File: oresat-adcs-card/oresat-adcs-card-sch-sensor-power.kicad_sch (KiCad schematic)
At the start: 83 parts, among them Q26 MOSFET-PCH-SOT23-6, Q27 MOSFET-PCH-SOT23-6, Q28 PMV45EN2R, Q29 PMV45EN2R, U29 MAX7310ATE, U30 MAX4211FETE, U31 TPS62111RSA, U32 MIC842LYC5-TR, U33 MIC842LYC5-TR

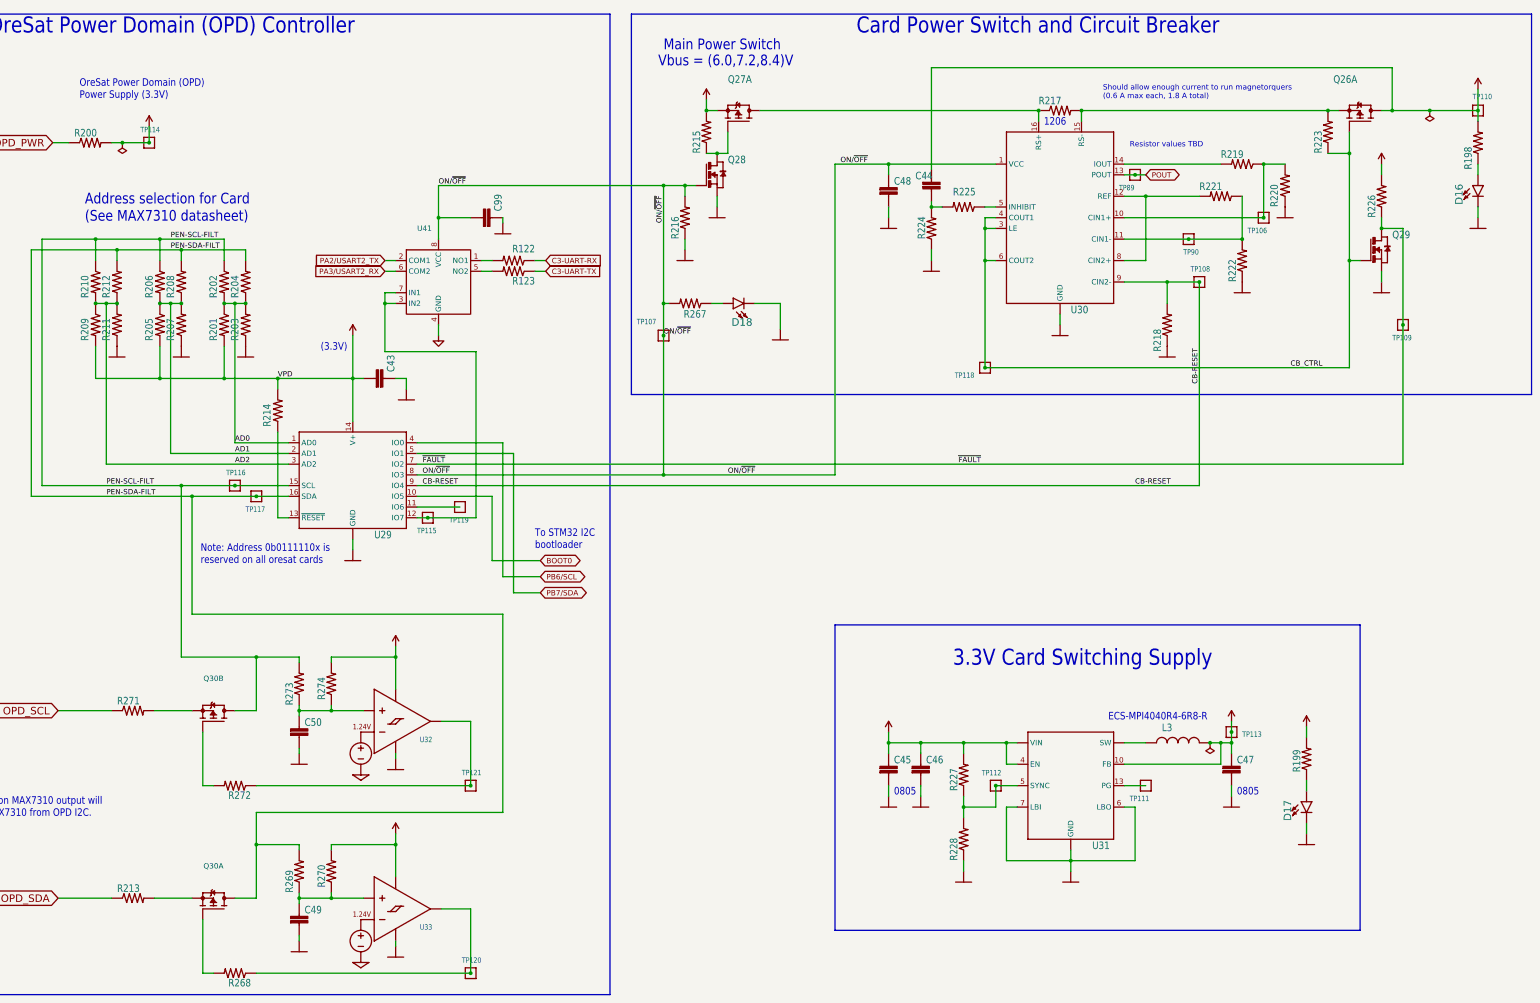
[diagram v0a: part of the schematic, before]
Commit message: Design review changes
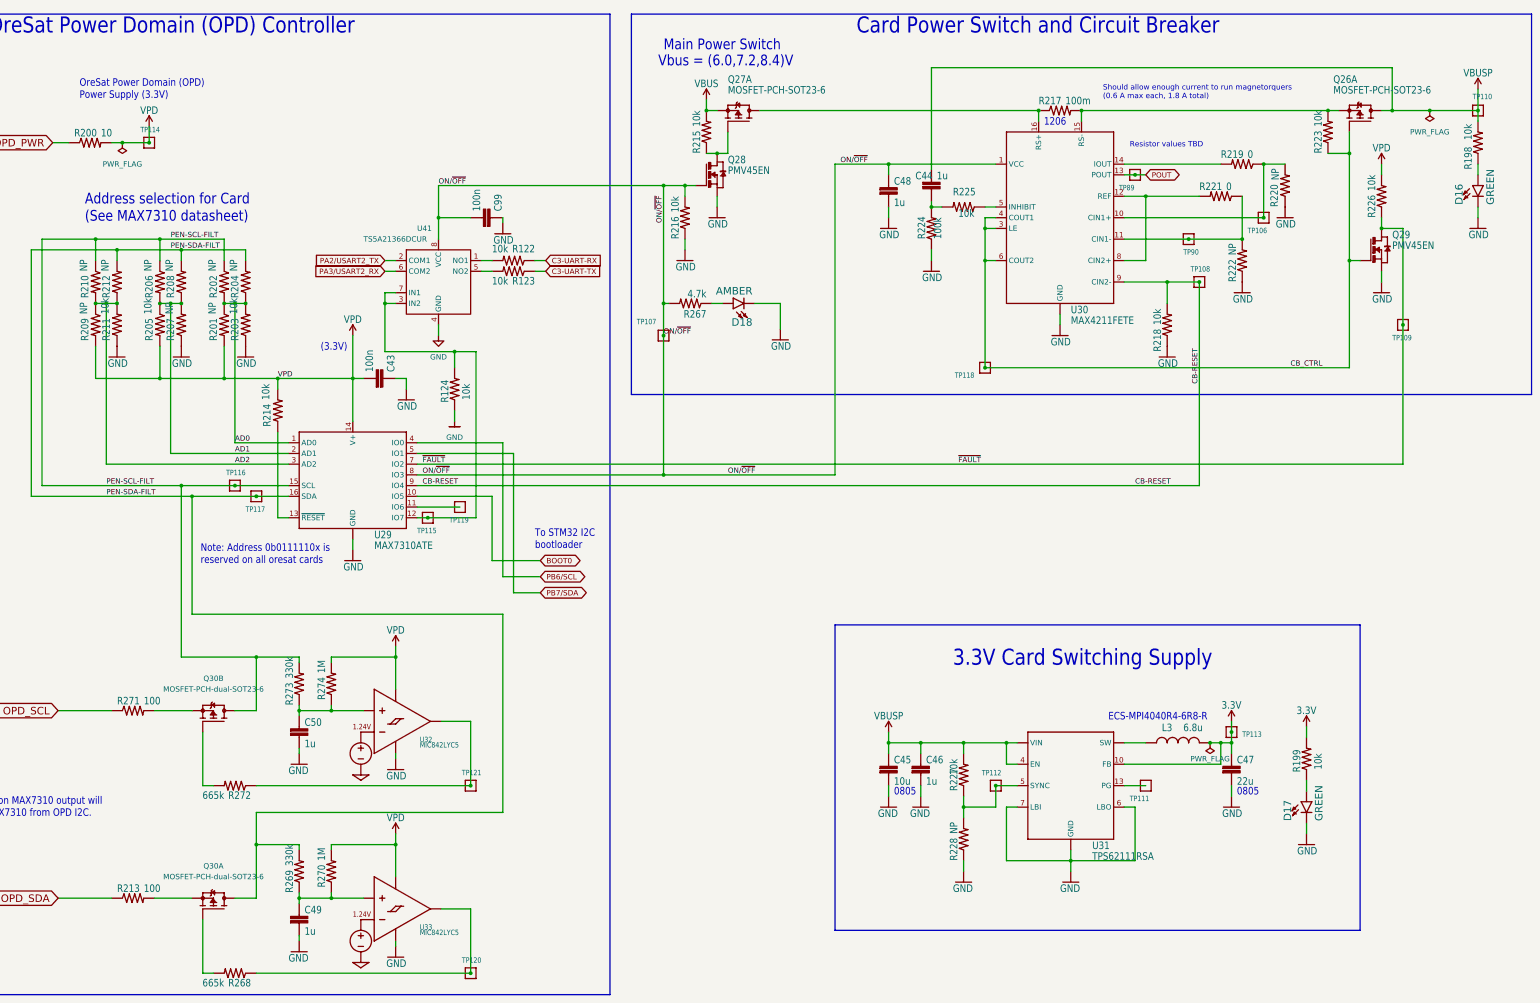
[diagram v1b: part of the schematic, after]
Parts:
- added R124: CRGCQ0603F2K7, oresat-acs-card:.0603-C-NOSILK, symbol oresat-acs-card-eagle-import:R-US_0603-C-NOSILK
- C43, C46, C48, C49, C50, C99, R122, R123, R198, R199, R200, R201, R202, R203, R204, R205, R206, R207, R208, R209, R210, R211, R212, R213, R214, R215, R216, R218, R219, R220, R221, R222, R223, R224, R225, R226, R227, R228, R267, R268, R269, R270, R271, R272, R273, R274: footprint (none) -> oresat-acs-card:.0603-C-NOSILK
- C44: value (none) -> 1u; footprint (none) -> oresat-acs-card:.0603-C-NOSILK
- C45, C47: footprint (none) -> oresat-acs-card:.0805-B-NOSILK
- D16, D17, D18: footprint (none) -> oresat-acs-card:LED-0603
- L3: footprint (none) -> oresat-acs-card:ECS-MPI4040
- Q26, Q27: footprint (none) -> oresat-acs-card:SOT23-6
- Q28, Q29: footprint (none) -> oresat-acs-card:SOT23
- Q30: value (none) -> MOSFET-PCH-dual-SOT23-6; footprint (none) -> oresat-acs-card:SOT23-6
- R217: footprint (none) -> oresat-acs-card:R1206
- TP106, TP107, TP108, TP109, TP110, TP111, TP112, TP113, TP114, TP115, TP116, TP117, TP118, TP119, TP120, TP121, TP89, TP90: value (none) -> TEST-POINT-LARGE-SQUARE; footprint (none) -> oresat-acs-card:1X01
- U29, U30: footprint (none) -> oresat-acs-card:QFN65P400X400X80-17T210
- U31: footprint (none) -> oresat-acs-card:S-PVQFN-16
- U32, U33: footprint (none) -> oresat-acs-card:SC70-5
- U41: value (none) -> TS5A21366DCUR; footprint (none) -> oresat-acs-card:DCU-R-PDSO-G8
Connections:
- net GND: now also R124.1
- net at TP115.1, U29.12 (IO7), U41.3 (IN2)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: now also R124.2

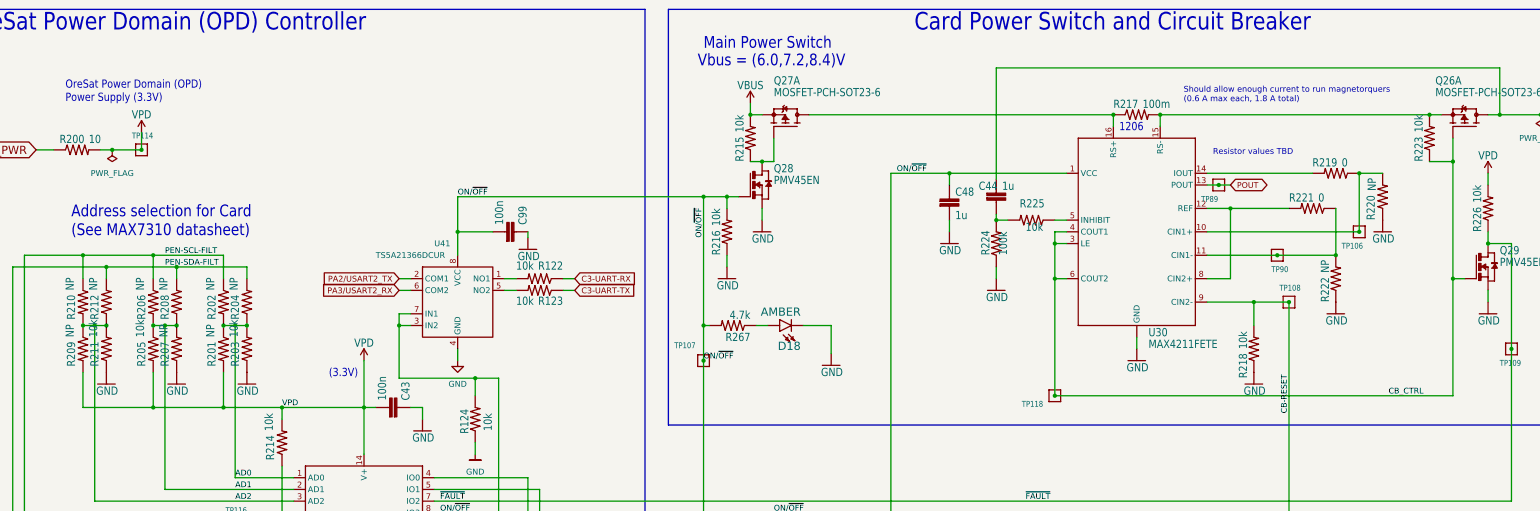
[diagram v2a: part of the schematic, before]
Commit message: Updated MT OPD breaker current limiting, and added OPD addresses to schematic
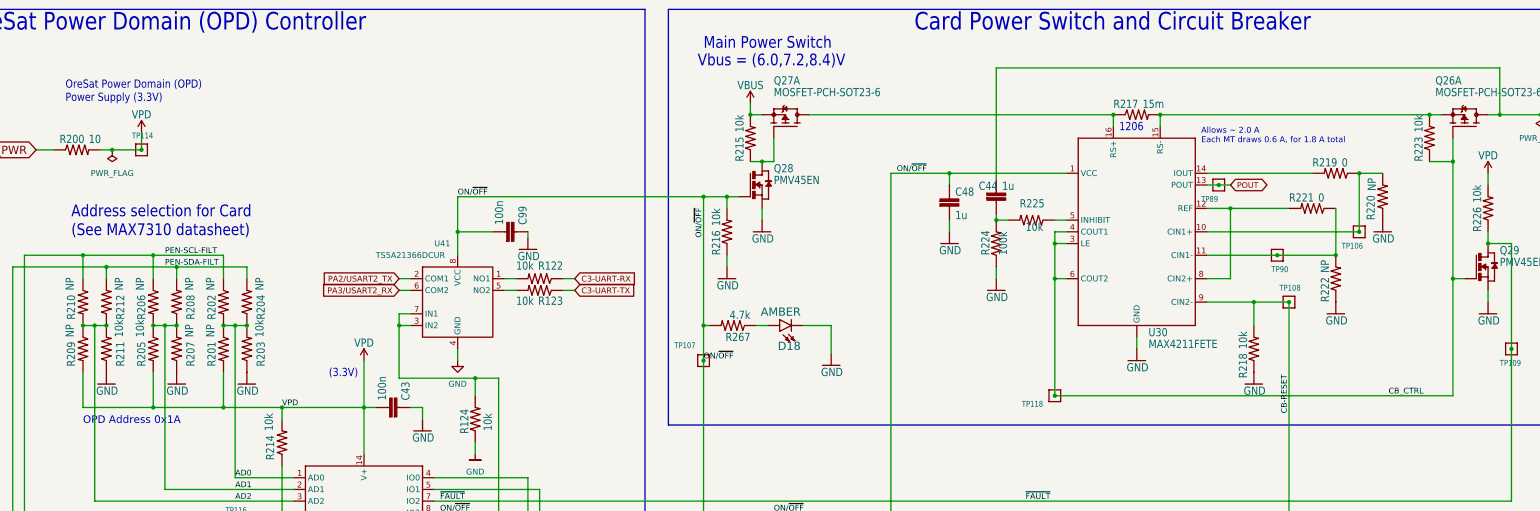
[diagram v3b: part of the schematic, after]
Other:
- note added: "Allows ~ 2.0 A Each MT draws 0.6 A, for 1.8 A total"
- note added: "OPD Address 0x1A"
- note removed: "Resistor values TBD"
- note removed: "Should allow enough current to run magnetorquers (0.6 A max each, 1.8 A total)"
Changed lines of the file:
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@@
     (stroke (width 0) (type default) (color 0 0 0 0))
+  )
+  (text "OPD Address 0x1A" (at 69.85 105.41 0)
+    (effects (font (size 1.651 1.651)) (justify left bottom))
   )
   (text "Vbus = (6.0,7.2,8.4)V" (at 203.2 27.94 180)
@@
     (effects (font (size 1.778 1.5113)) (justify left bottom))
   )
-  (text "Should allow enough current to run magnetorquers\n(0.6 A max each, 1.8 A total)"
-    (at 308.61 35.56 0)
+  (text "Allows ~ 2.0 A\nEach MT draws 0.6 A, for 1.8 A total"
+    (at 312.42 44.45 0)
     (effects (font (size 1.27 1.27)) (justify left bottom))
   )
@@
   (text "To STM32 I2C\nbootloader" (at 173.99 142.24 180)
     (effects (font (size 1.778 1.5113)) (justify left bottom))
-  )
-  (text "Resistor values TBD" (at 314.96 46.99 0)
-    (effects (font (size 1.27 1.27)) (justify left bottom))
   )
   (text "Address selection for Card\n(See MAX7310 datasheet)"
@@
   (symbol (lib_id "oresat-acs-card-eagle-import:R-US_0603-C-NOSILK") (at 90.17 78.74 90) (unit 1)
     (in_bom yes) (on_board yes)
-    (property "Reference" "R208" (id 0) (at 88.6714 82.55 0)
-      (effects (font (size 1.778 1.5113)) (justify left bottom))
-    )
-    (property "Value" "NP" (id 1) (at 88.392 76.2 0)
+    (property "Reference" "R208" (id 0) (at 94.2594 82.55 0)
+      (effects (font (size 1.778 1.5113)) (justify left bottom))
+    )
+    (property "Value" "NP" (id 1) (at 93.98 76.2 0)
       (effects (font (size 1.778 1.5113)) (justify left bottom))
     )
@@
   (symbol (lib_id "oresat-acs-card-eagle-import:R-US_0603-C-NOSILK") (at 74.93 78.74 90) (unit 1)
     (in_bom yes) (on_board yes)
-    (property "Reference" "R212" (id 0) (at 73.4314 82.55 0)
-      (effects (font (size 1.778 1.5113)) (justify left bottom))
-    )
-    (property "Value" "NP" (id 1) (at 73.152 76.2 0)
+    (property "Reference" "R212" (id 0) (at 79.0194 82.55 0)
+      (effects (font (size 1.778 1.5113)) (justify left bottom))
+    )
+    (property "Value" "NP" (id 1) (at 78.74 76.2 0)
       (effects (font (size 1.778 1.5113)) (justify left bottom))
     )
@@
   (symbol (lib_id "oresat-acs-card-eagle-import:R-US_0603-C-NOSILK") (at 90.17 88.9 90) (unit 1)
     (in_bom yes) (on_board yes)
-    (property "Reference" "R207" (id 0) (at 88.6714 92.71 0)
-      (effects (font (size 1.778 1.5113)) (justify left bottom))
-    )
-    (property "Value" "NP" (id 1) (at 88.392 86.36 0)
+    (property "Reference" "R207" (id 0) (at 94.2594 92.71 0)
+      (effects (font (size 1.778 1.5113)) (justify left bottom))
+    )
+    (property "Value" "NP" (id 1) (at 93.98 86.36 0)
       (effects (font (size 1.778 1.5113)) (justify left bottom))
     )
@@
   (symbol (lib_id "oresat-acs-card-eagle-import:R-US_0603-C-NOSILK") (at 105.41 88.9 90) (unit 1)
     (in_bom yes) (on_board yes)
-    (property "Reference" "R203" (id 0) (at 103.9114 92.71 0)
-      (effects (font (size 1.778 1.5113)) (justify left bottom))
-    )
-    (property "Value" "10k" (id 1) (at 103.632 86.36 0)
+    (property "Reference" "R203" (id 0) (at 109.4994 92.71 0)
+      (effects (font (size 1.778 1.5113)) (justify left bottom))
+    )
+    (property "Value" "10k" (id 1) (at 109.22 86.36 0)
       (effects (font (size 1.778 1.5113)) (justify left bottom))
     )
@@
       (effects (font (size 1.778 1.5113)) (justify left bottom))
     )
-    (property "Value" "100m" (id 1) (at 299.72 36.83 0)
+    (property "Value" "15m" (id 1) (at 299.72 36.83 0)
       (effects (font (size 1.778 1.5113)) (justify left bottom))
     )
@@
   (symbol (lib_id "oresat-acs-card-eagle-import:R-US_0603-C-NOSILK") (at 105.41 78.74 90) (unit 1)
     (in_bom yes) (on_board yes)
-    (property "Reference" "R204" (id 0) (at 103.9114 82.55 0)
-      (effects (font (size 1.778 1.5113)) (justify left bottom))
-    )
-    (property "Value" "NP" (id 1) (at 103.632 76.2 0)
+    (property "Reference" "R204" (id 0) (at 109.4994 82.55 0)
+      (effects (font (size 1.778 1.5113)) (justify left bottom))
+    )
+    (property "Value" "NP" (id 1) (at 109.22 76.2 0)
       (effects (font (size 1.778 1.5113)) (justify left bottom))
     )
@@
   (symbol (lib_id "oresat-acs-card-eagle-import:R-US_0603-C-NOSILK") (at 74.93 88.9 90) (unit 1)
     (in_bom yes) (on_board yes)
-    (property "Reference" "R211" (id 0) (at 73.4314 92.71 0)
-      (effects (font (size 1.778 1.5113)) (justify left bottom))
-    )
-    (property "Value" "10k" (id 1) (at 73.152 86.36 0)
-      (effects (font (size 1.778 1.5113)) (justify left bottom))
-    )
+    (property "Reference" "R211" (id 0) (at 79.0194 92.71 0)
+      (effects (font (size 1.778 1.5113)) (justify left bottom))
+    )
+    (property "Value" "10k" (id 1) (at 78.74 86.36 0)
+      (effects (font (size 1.778 1.5113)) (justify left bottom))
+    )

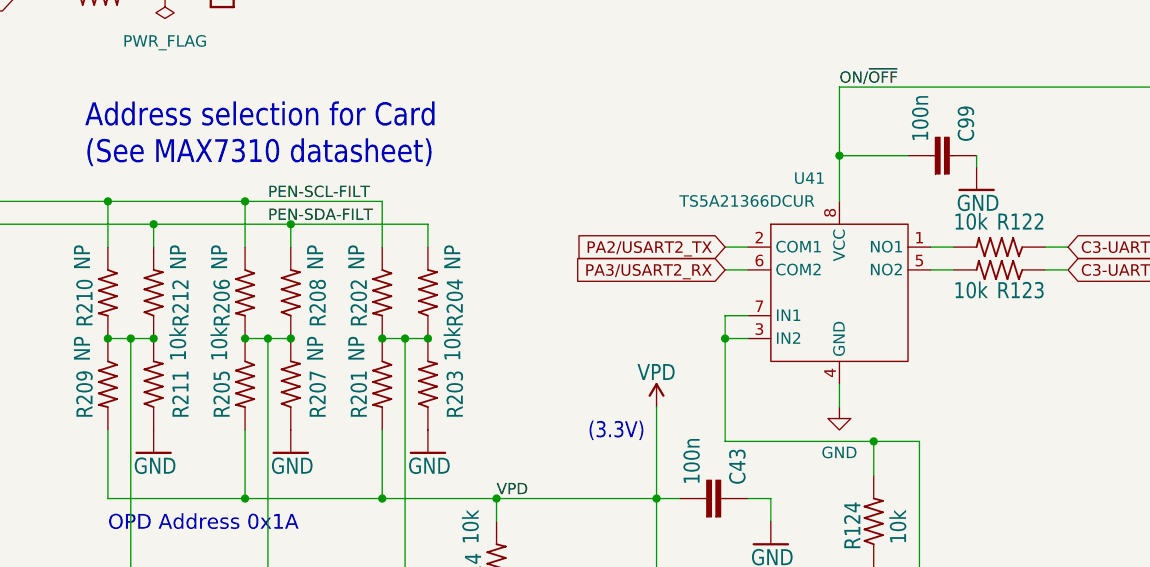
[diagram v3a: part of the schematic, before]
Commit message: Fixed ADCS card issues
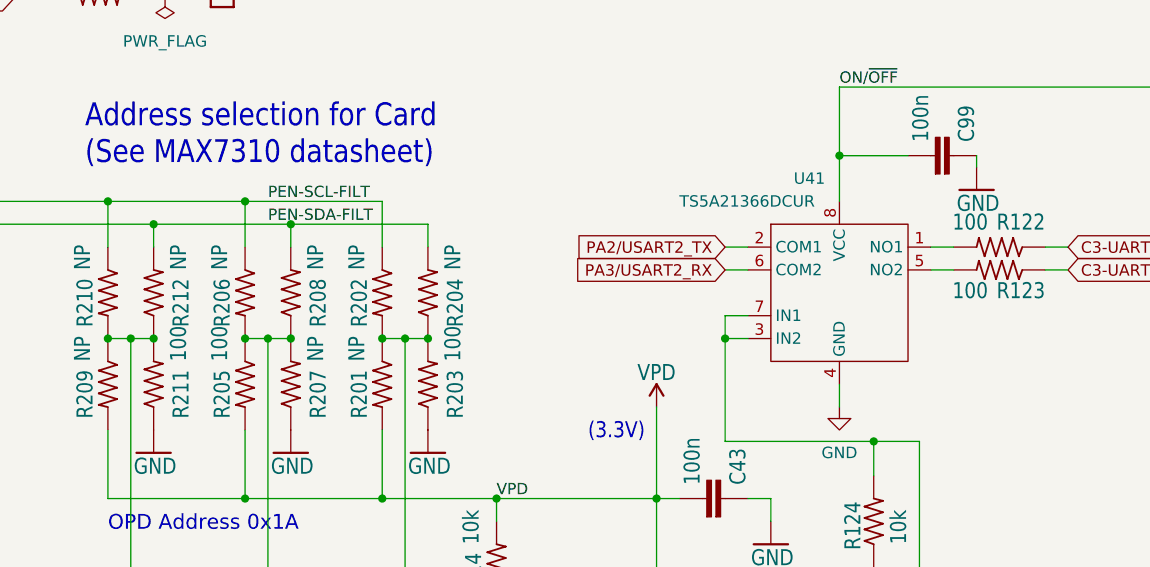
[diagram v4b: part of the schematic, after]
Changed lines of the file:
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@@
       (effects (font (size 1.778 1.5113)) (justify right top))
     )
-    (property "Value" "10k" (id 1) (at 83.312 86.36 0)
+    (property "Value" "100" (id 1) (at 83.312 86.36 0)
       (effects (font (size 1.778 1.5113)) (justify right top))
     )
@@
       (effects (font (size 1.778 1.5113)) (justify left bottom))
     )
-    (property "Value" "10k" (id 1) (at 109.22 86.36 0)
+    (property "Value" "100" (id 1) (at 109.22 86.36 0)
       (effects (font (size 1.778 1.5113)) (justify left bottom))
     )
@@
       (effects (font (size 1.778 1.5113)) (justify left bottom))
     )
-    (property "Value" "10k" (id 1) (at 167.64 77.47 0)
+    (property "Value" "100" (id 1) (at 167.64 77.47 0)
       (effects (font (size 1.778 1.5113)) (justify left bottom))
     )
@@
       (effects (font (size 1.778 1.5113)) (justify left bottom))
     )
-    (property "Value" "10k" (id 1) (at 167.64 69.85 0)
+    (property "Value" "100" (id 1) (at 167.64 69.85 0)
       (effects (font (size 1.778 1.5113)) (justify left bottom))
     )
@@
       (effects (font (size 1.778 1.5113)) (justify left bottom))
     )
-    (property "Value" "10k" (id 1) (at 78.74 86.36 0)
-      (effects (font (size 1.778 1.5113)) (justify left bottom))
-    )
+    (property "Value" "100" (id 1) (at 78.74 86.36 0)
+      (effects (font (size 1.778 1.5113)) (justify left bottom))
+    )

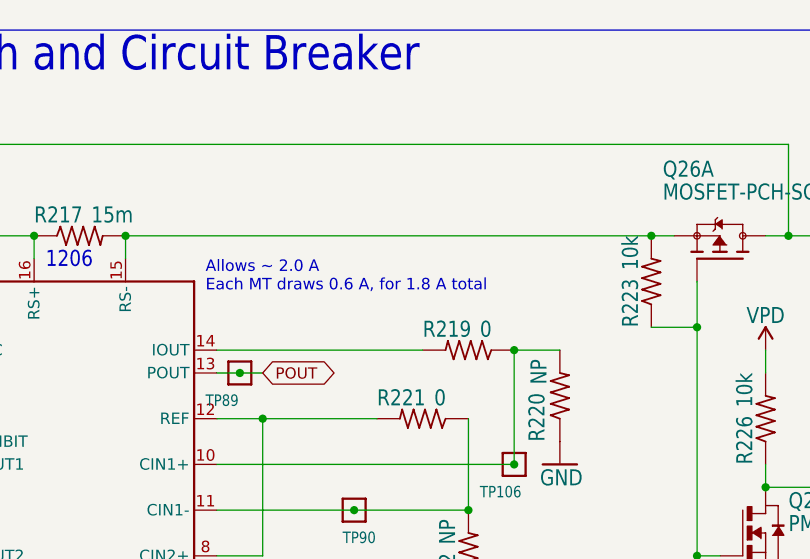
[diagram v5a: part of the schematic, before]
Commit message: Changed MT current limit setting, and added filter for current sense to ADC
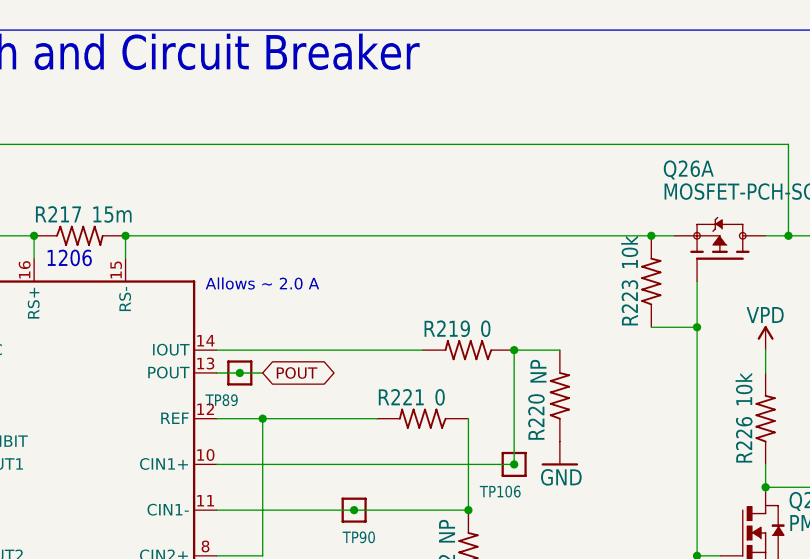
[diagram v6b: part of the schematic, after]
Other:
- note added: "Allows ~ 2.0 A"
- note removed: "Allows ~ 2.0 A Each MT draws 0.6 A, for 1.8 A total"
